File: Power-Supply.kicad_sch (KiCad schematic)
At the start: 72 parts, among them J2 ADC1, J3 ADC2, J4 DAC1, J5 DAC2, J6 DAC3, J7 FPGA, J8 Frontpanel, J9 RPT-75C, U1 LT3081xR, U2 LT3081xR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

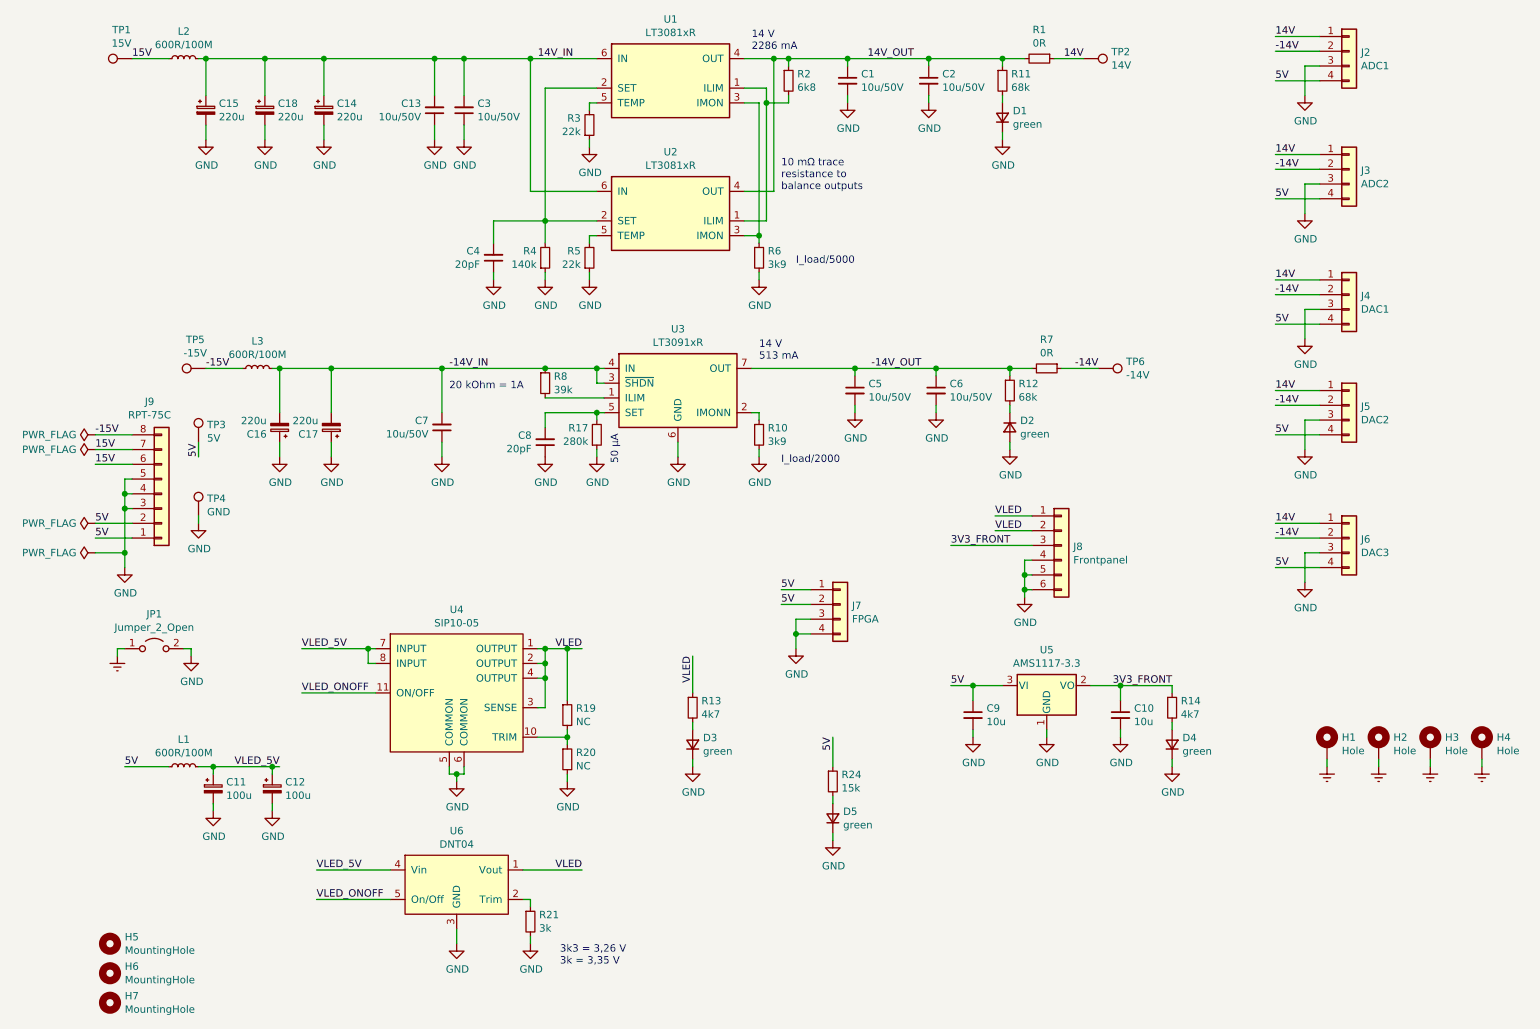
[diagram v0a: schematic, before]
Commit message: Update to KiCad 6
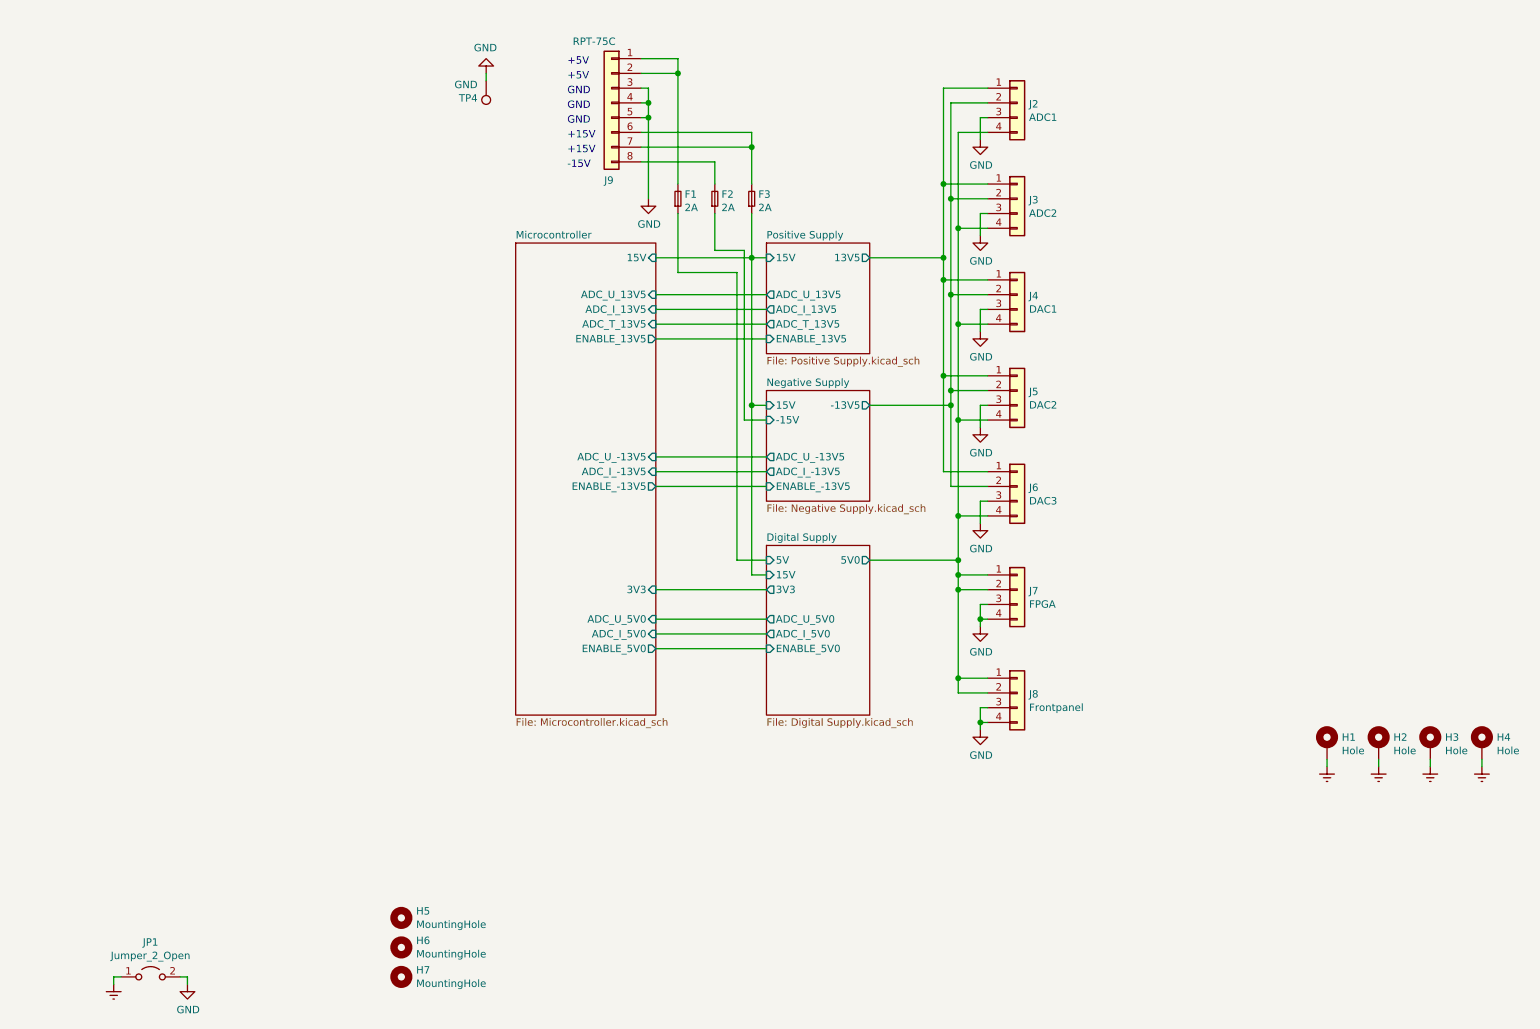
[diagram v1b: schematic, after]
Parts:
- removed C1, C13, C2, C3, C5, C6, C7: 10u/50V, Capacitor_SMD:C_1206_3216Metric, symbol Device:C_Small
- removed C10, C9: 10u, Capacitor_SMD:C_0805_2012Metric, symbol Device:C_Small
- removed C11, C12: 100u, Capacitor_Tantalum_SMD:CP_EIA-3528-21_Kemet-B, symbol Device:C_Polarized_Small
- removed C14, C15, C16, C17, C18: 220u, Capacitor_THT:CP_Radial_D6.3mm_P2.50mm, symbol Device:C_Polarized_Small
- removed C4, C8: 20pF, Capacitor_SMD:C_0603_1608Metric, symbol Device:C_Small
- removed D1, D2, D3, D4, D5: green, LED_SMD:LED_0603_1608Metric, symbol Device:D_Small
- removed J8: Frontpanel, Connector_JST:JST_VH_B6P-VH_1x06_P3.96mm_Vertical, symbol Connector_Generic:Conn_01x06
- removed L1, L2, L3: 600R/100M, Inductor_SMD:L_0805_2012Metric, symbol Device:L_Small
- removed R1, R7: 0R, Resistor_SMD:R_0603_1608Metric, symbol Device:R_Small
- removed R10, R6: 3k9, Resistor_SMD:R_0603_1608Metric, symbol Device:R_Small
- removed R11, R12: 68k, Resistor_SMD:R_0603_1608Metric, symbol Device:R_Small
- removed R13, R14: 4k7, Resistor_SMD:R_0603_1608Metric, symbol Device:R_Small
- removed R17: 280k, Resistor_SMD:R_0603_1608Metric, symbol Device:R_Small
- removed R19, R20: NC, Resistor_SMD:R_0603_1608Metric, symbol Device:R_Small
- removed R2: 6k8, Resistor_SMD:R_0603_1608Metric, symbol Device:R_Small
- removed R21: 3k, Resistor_SMD:R_0603_1608Metric, symbol Device:R_Small
- removed R24: 15k, Resistor_SMD:R_0603_1608Metric, symbol Device:R_Small
- removed R3, R5: 22k, Resistor_SMD:R_0603_1608Metric, symbol Device:R_Small
- removed R4: 140k, Resistor_SMD:R_0603_1608Metric, symbol Device:R_Small
- removed R8: 39k, Resistor_SMD:R_0603_1608Metric, symbol Device:R_Small
- removed TP1: 15V, TestPoint:TestPoint_Pad_D2.0mm, symbol Connector:TestPoint
- removed TP2: 14V, TestPoint:TestPoint_Pad_D2.0mm, symbol Connector:TestPoint
- removed TP3: 5V, TestPoint:TestPoint_Pad_D2.0mm, symbol Connector:TestPoint
- removed TP5: -15V, TestPoint:TestPoint_Pad_D2.0mm, symbol Connector:TestPoint
- removed TP6: -14V, TestPoint:TestPoint_Pad_D2.0mm, symbol Connector:TestPoint
- removed U1, U2: LT3081xR, Package_TO_SOT_SMD:TO-263-7_TabPin4, symbol twam-Misc:LT3081xR
- removed U3: LT3091xR, Package_TO_SOT_SMD:TO-263-7_TabPin4, symbol twam-Misc:LT3091xR
- removed U4: SIP10-05, twam-Misc:SIP10-05, symbol twam-Misc:SIP10-05
- removed U5: AMS1117-3.3, Package_TO_SOT_SMD:SOT-223-3_TabPin2, symbol Regulator_Linear:AMS1117-3.3
- removed U6: DNT04, twam-Misc:DNT04, symbol twam-Misc:DNT04
- added F1, F2, F3: 2A, Fuse:Fuse_0603_1608Metric_Pad1.05x0.95mm_HandSolder, symbol Device:Fuse_Small
- added J8: Frontpanel, Connector_JST:JST_VH_B4P-VH_1x04_P3.96mm_Vertical, symbol Connector_Generic:Conn_01x04
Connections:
- net GND: now also J8.3 (Pin_3), J8.4 (Pin_4)
- net -14V renamed Negative Supply/-13V5
- net -15V: no longer names the net of J9.8 (Pin_8)
- net -15V: now also F2.2
- net 14V renamed Positive Supply/13V5
- net 15V: no longer names the net of J9.6 (Pin_6), J9.7 (Pin_7)
- net 15V: now also F3.2
- net 5V renamed Digital Supply/5V0
- net Digital Supply/5V0: now also J8.1 (Pin_1), J8.2 (Pin_2); no longer J9.1 (Pin_1), J9.2 (Pin_2)
- new net: F1.2, J9.1 (Pin_1), J9.2 (Pin_2)
- new net Digital Supply/15V: F3.1
- new net Digital Supply/5V: F1.1
- new net Negative Supply/-15V: F2.1
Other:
- added sheet Digital Supply (Digital Supply.kicad_sch)
- added sheet Microcontroller (Microcontroller.kicad_sch)
- added sheet Negative Supply (Negative Supply.kicad_sch)
- added sheet Positive Supply (Positive Supply.kicad_sch)
- note added: "+15V"
- note added: "+5V"
- note added: "-15V"
- note added: "GND"
- note removed: "10 mΩ trace resistance to balance outputs"
- note removed: "14 V 2286 mA"
- note removed: "14 V 513 mA"
- note removed: "20 kOhm = 1A"
- note removed: "3k3 = 3,26 V 3k = 3,35 V"
- note removed: "50 µA"
- note removed: "I_load/2000"
- note removed: "I_load/5000"
- moved on the sheet: H5, H6, H7, J2, J3, J4, J5, J6, J7, J9, JP1, TP4
